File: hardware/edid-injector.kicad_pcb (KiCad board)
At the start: 2 copper layers, 42 parts, among them SW1 SW_PUSH, U1 C8051F381/3/5/7/C-GQ

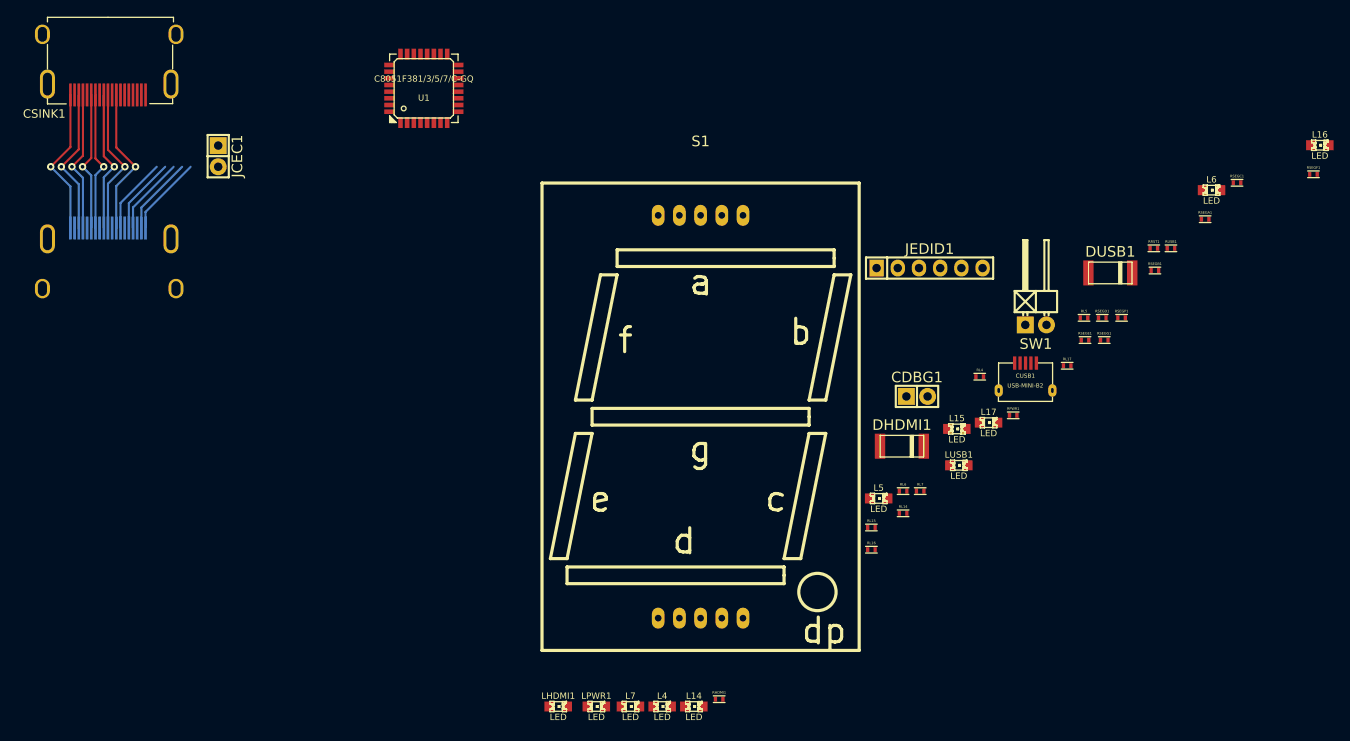
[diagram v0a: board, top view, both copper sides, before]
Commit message: Begin PCB layout - cleaning up rats nest
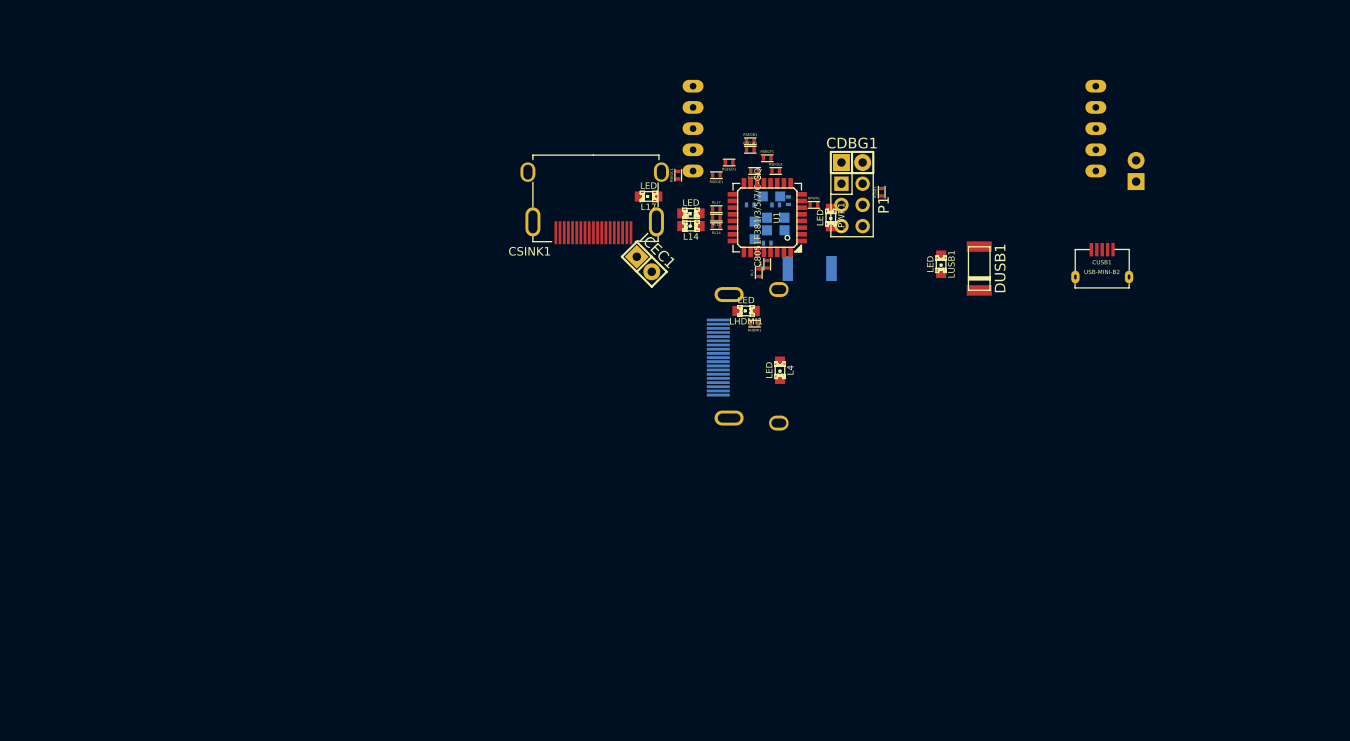
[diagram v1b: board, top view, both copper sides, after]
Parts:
- removed JEDID1: CONN_01X06, Pin_Headers:Pin_Header_Straight_1x06
- added P1: CONN_02X03, Pin_Headers:Pin_Header_Straight_2x03, F.Cu at (141.7, 67.8)
- DHDMI1, L16, L5, L6, L7, RL16, RL5, RL6, RRST1, S1, SW1: moved to B.Cu
- moved CSRC1 75.8 mm to (127.0, 86.1), turned to 270 degrees
- moved RSEGC1 67.0 mm to (120.9, 64.3), turned to 90 degrees
- moved L16 65.8 mm to (132.6, 69.3), turned to 180 degrees
- moved RSEGF1 65.5 mm to (131.6, 62.2)
- moved LPWR1 65.0 mm to (139.2, 69.3), turned to 270 degrees
- moved CSINK1 60.5 mm to (110.7, 69.8)
- moved L7 59.0 mm to (130.0, 70.9), turned to 90 degrees
- moved L14 57.6 mm to (122.4, 70.4), turned to 180 degrees
- moved RSEGA1 55.1 mm to (129.5, 61.2)
- moved JCEC1 52.7 mm to (116.8, 74.9), turned to 315 degrees
- moved LHDMI1 52.5 mm to (129.0, 80.5), turned to 180 degrees
- moved L6 52.4 mm to (132.6, 70.9)
- moved RSEGB1 50.9 mm to (129.5, 60.2)
- moved L17 48.9 mm to (117.3, 66.8), turned to 180 degrees
- moved RSEGD1 48.4 mm to (127.0, 62.7), turned to 180 degrees
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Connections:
- CSINK1 pad 14: Net-(CSINK1-Pad14) -> (no net)
- CSRC1 pad 14: Net-(CSRC1-Pad14) -> (no net)
- CUSB1 pad 4: Net-(CUSB1-Pad4) -> (no net)
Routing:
- net /D2+: track 17.9 -> 0.00 mm, vias 1 -> 0
- net /CLK-: track 17.8 -> 0.00 mm, vias 1 -> 0
- net /D2-: track 17.7 -> 0.00 mm, vias 1 -> 0
- net /CLK+: track 17.6 -> 0.00 mm, vias 1 -> 0
- net /D1+: track 17.0 -> 0.00 mm, vias 1 -> 0
- net /D0-: track 17.0 -> 0.00 mm, vias 1 -> 0
- net /D1-: track 16.8 -> 0.00 mm, vias 1 -> 0
- net /D0+: track 16.8 -> 0.00 mm, vias 1 -> 0
- net /SRC_HPD: track 9.58 -> 0.00 mm
- net /VHDMI: track 9.36 -> 0.00 mm
- net /SRC_SDA: track 9.35 -> 0.00 mm
- net /SRC_SCL: track 9.14 -> 0.00 mm
- net /SRC_CEC: track 9.13 -> 0.00 mm

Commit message: Converging on sane placement for parts
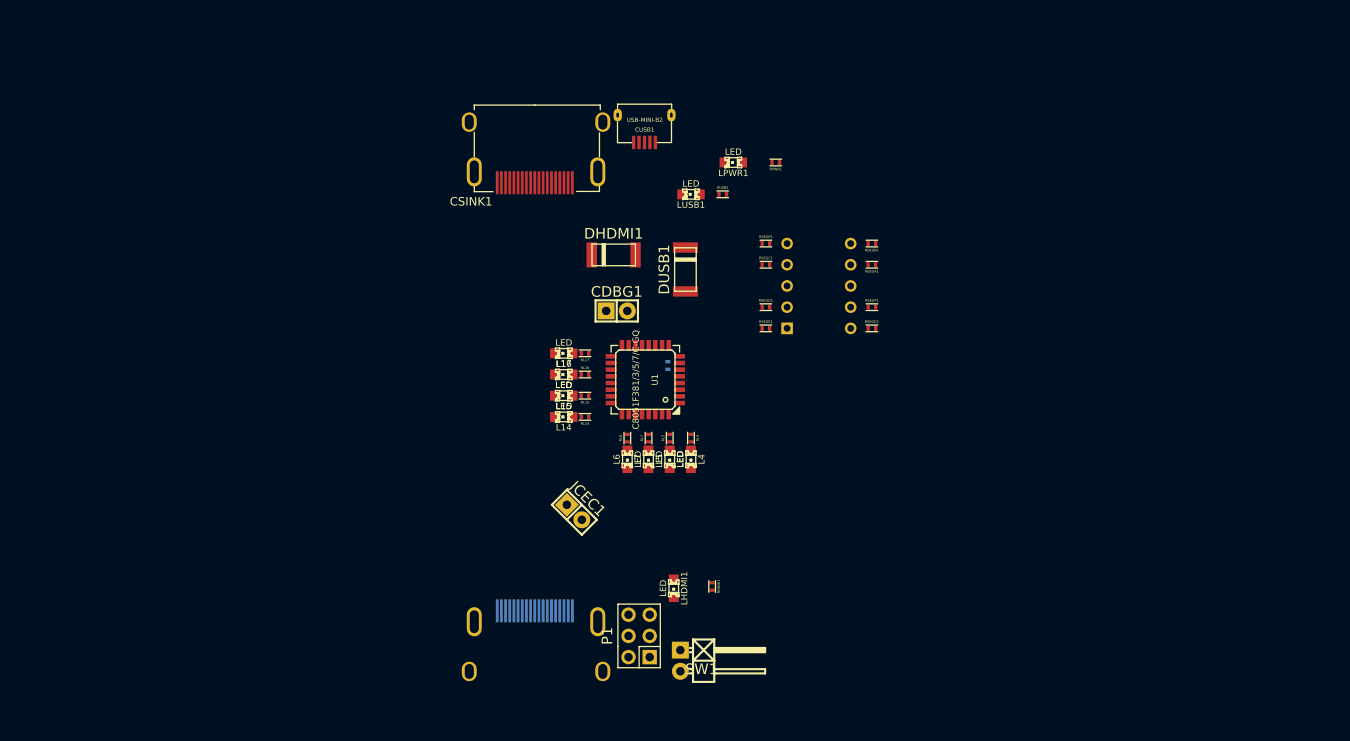
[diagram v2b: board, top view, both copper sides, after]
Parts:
- DHDMI1, L16, L5, L6, L7, RL16, RL5, RL6, SW1: moved to F.Cu
- S1: footprint Displays_7-Segment:7SegmentLED_SBC18-11EGWA -> Sockets_DIP:DIP-10__300
- moved SW1 80.2 mm to (121.2, 122.4), turned to 270 degrees
- moved CUSB1 58.2 mm to (116.9, 57.1), turned to 180 degrees
- moved P1 57.6 mm to (116.2, 119.5), turned to 90 degrees
- moved CSRC1 39.3 mm to (103.7, 117.8), turned to 180 degrees
- moved DUSB1 35.2 mm to (121.8, 75.6), turned to 90 degrees
- moved LHDMI1 34.4 mm to (120.4, 113.8), turned to 270 degrees
- moved L5 33.8 mm to (119.9, 98.3), turned to 270 degrees
- moved CDBG1 33.3 mm to (113.5, 80.5)
- moved L6 32.7 mm to (114.8, 98.3), turned to 270 degrees
- moved RHDMI1 31.9 mm to (125.0, 113.5), turned to 270 degrees
- moved L16 31.6 mm to (107.2, 88.1)
- moved LUSB1 31.1 mm to (122.4, 66.5), turned to 180 degrees
- moved JCEC1 30.9 mm to (108.5, 104.6)
- moved RL5 30.7 mm to (119.9, 95.8), turned to 270 degrees
- moved L7 30.2 mm to (117.3, 98.3), turned to 270 degrees
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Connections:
- CSINK1 pad 14: (no net) -> Net-(CSINK1-Pad14)
- CSRC1 pad 14: (no net) -> Net-(CSRC1-Pad14)
- CUSB1 pad 4: (no net) -> Net-(CUSB1-Pad4)
- P1 pad 1: (no net) -> Net-(P1-Pad1)
- P1 pad 2: (no net) -> Net-(P1-Pad2)
- P1 pad 3: (no net) -> Net-(P1-Pad3)
- P1 pad 4: (no net) -> Net-(P1-Pad4)
- P1 pad 6: (no net) -> Net-(P1-Pad6)

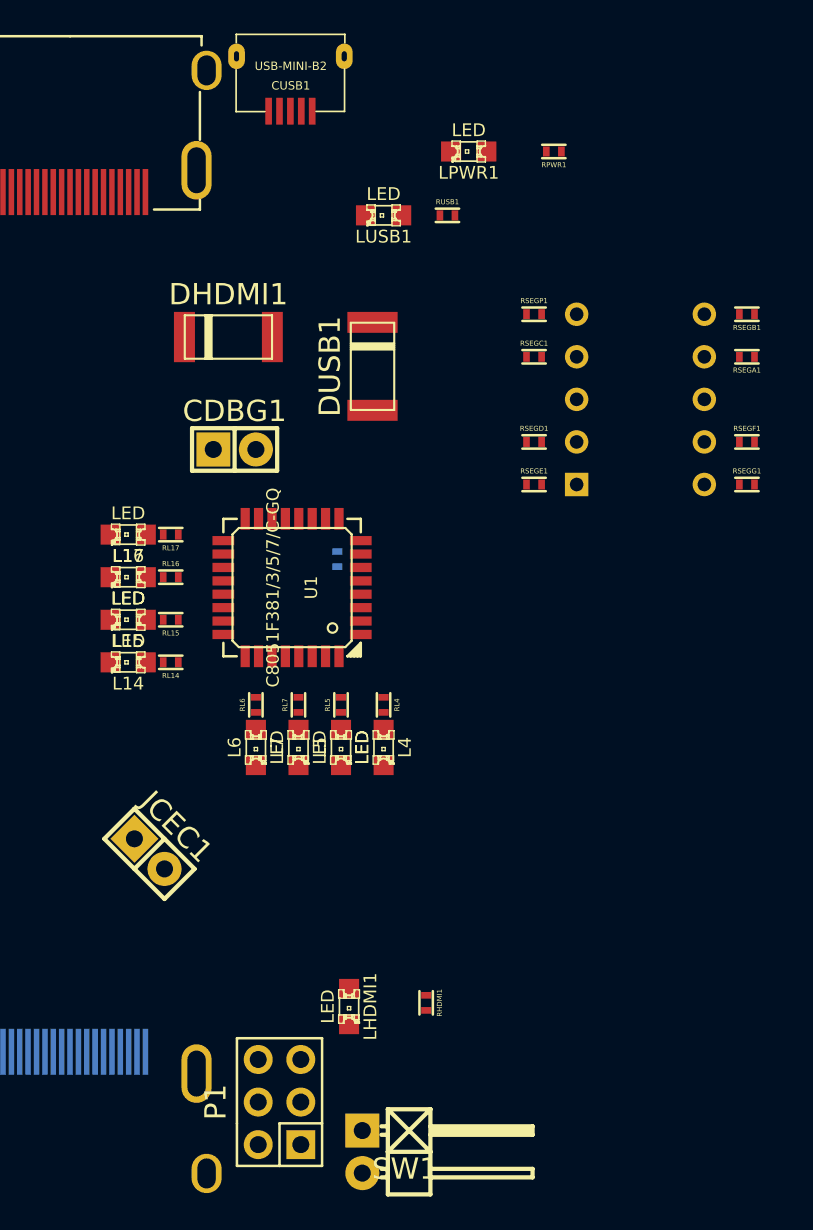
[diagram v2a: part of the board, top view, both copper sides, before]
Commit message: Closer to an autorouter-friendly layout.
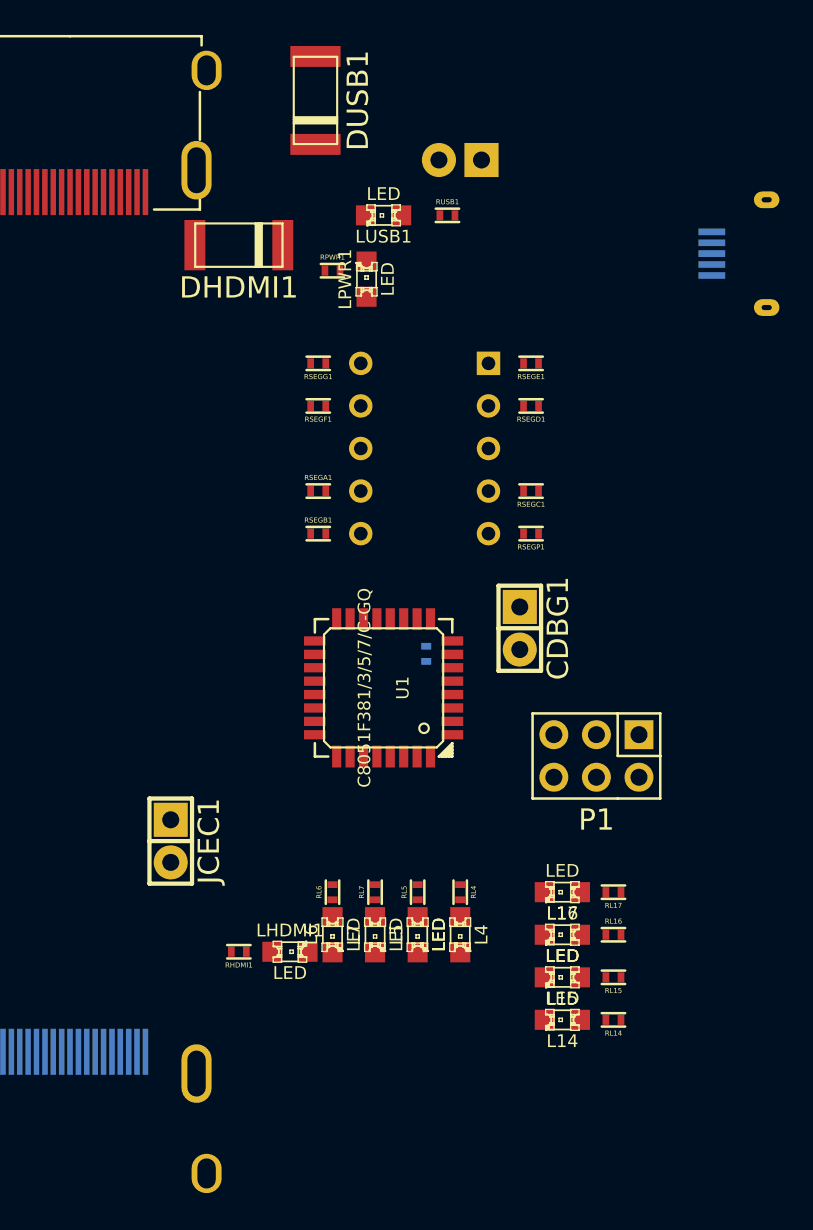
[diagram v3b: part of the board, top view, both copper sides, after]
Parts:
- CUSB1, SW1: moved to B.Cu
- moved SW1 59.5 mm to (127.0, 63.2), turned to 180 degrees
- moved RL14 34.0 mm to (136.1, 114.6)
- moved RL15 34.0 mm to (136.1, 112.0)
- moved RL16 34.0 mm to (136.1, 109.5)
- moved RL17 34.0 mm to (136.1, 106.9)
- moved L14 33.6 mm to (133.1, 114.6)
- moved L15 33.6 mm to (133.1, 112.0)
- moved L16 33.6 mm to (133.1, 109.5)
- moved L17 33.6 mm to (133.1, 106.9)
- moved CUSB1 30.8 mm to (145.3, 68.8), turned to 270 degrees
- moved RSEGB1 28.7 mm to (118.5, 85.5), turned to 0 degrees
- moved P1 28.0 mm to (135.1, 98.8), turned to 180 degrees
- moved RSEGA1 26.8 mm to (118.5, 83.0), turned to 0 degrees
- moved RSEGG1 26.6 mm to (118.5, 75.4), turned to 180 degrees
- moved RSEGF1 25.7 mm to (118.5, 77.9), turned to 180 degrees
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
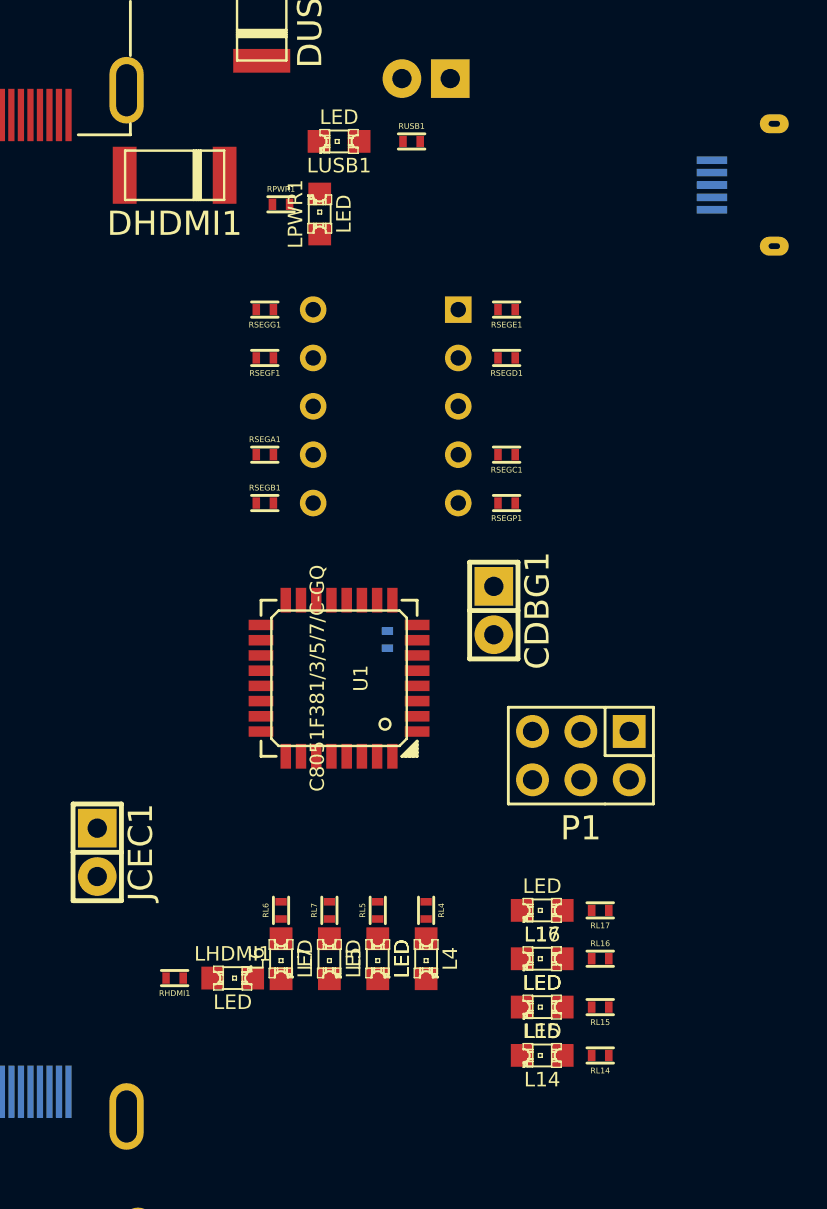
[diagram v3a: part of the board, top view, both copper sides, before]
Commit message: Better layout for PCB - autorouter is at -7 traces
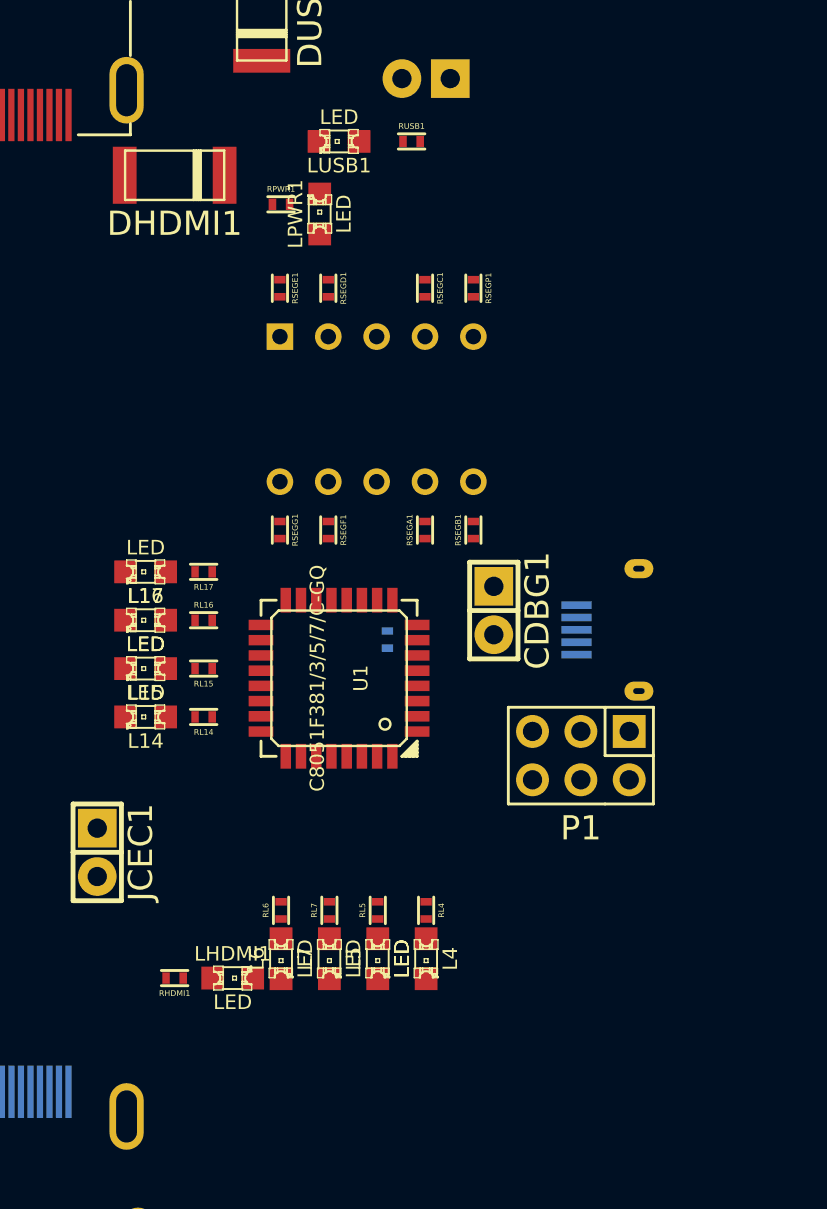
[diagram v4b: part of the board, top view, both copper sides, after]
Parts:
- moved L14 27.4 mm to (112.3, 96.8)
- moved L15 27.4 mm to (112.3, 94.2)
- moved L16 27.4 mm to (112.3, 91.7)
- moved L17 27.4 mm to (112.3, 89.2)
- moved RL14 27.4 mm to (115.3, 96.8)
- moved RL15 27.4 mm to (115.3, 94.2)
- moved RL16 27.4 mm to (115.3, 91.7)
- moved RL17 27.4 mm to (115.3, 89.2)
- moved CUSB1 24.4 mm to (138.2, 92.2)
- moved RSEGE1 12.0 mm to (119.3, 74.3), turned to 270 degrees
- moved RSEGG1 11.6 mm to (119.3, 87.0), turned to 270 degrees
- moved RSEGP1 11.4 mm to (129.5, 74.3), turned to 270 degrees
- moved RSEGB1 11.0 mm to (129.5, 87.0), turned to 90 degrees
- moved RSEGD1 10.1 mm to (121.9, 74.3), turned to 270 degrees
- moved RSEGC1 9.74 mm to (126.9, 74.3), turned to 270 degrees
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
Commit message: Preliminary route.
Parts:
- moved JCEC1 3.05 mm to (106.7, 103.9)
- moved L15 0.51 mm to (112.3, 94.7)
- moved L17 0.51 mm to (112.3, 89.7)
- moved LHDMI1 0.51 mm to (116.8, 111.0)
- moved RHDMI1 0.51 mm to (113.8, 111.0)
- moved RL15 0.51 mm to (115.3, 94.7)
- moved RL17 0.51 mm to (115.3, 89.7)
- moved RRST1 0.51 mm to (125.0, 93.2)
- moved RSEGC1 0.51 mm to (126.9, 74.8)
- moved RSEGD1 0.51 mm to (121.9, 74.8)
- moved RSEGE1 0.51 mm to (119.3, 74.8)
- moved RSEGP1 0.51 mm to (129.5, 74.8)
- moved CDBG1 0.51 mm to (130.6, 91.7)
- moved CUSB1 0.51 mm to (138.2, 92.7)
- moved L14 0.51 mm to (112.3, 97.3)
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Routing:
- net GND: track 0.00 -> 239.2 mm, vias 0 -> 6
- net /SINK_SCL: track 0.00 -> 83.0 mm, vias 0 -> 2
- net /CLK-: track 0.00 -> 71.5 mm, vias 0 -> 3
- net /D0+: track 0.00 -> 67.4 mm, vias 0 -> 3
- net /D1-: track 0.00 -> 64.1 mm, vias 0 -> 1
- net Net-(CDBG1-Pad2): track 0.00 -> 61.6 mm, vias 0 -> 4
- net /VHDMI: track 0.00 -> 59.6 mm, vias 0 -> 1
- net /D1+: track 0.00 -> 59.5 mm, vias 0 -> 1
- net /SINK_CEC: track 0.00 -> 57.7 mm, vias 0 -> 3
- net /VUSB: track 0.00 -> 54.5 mm, vias 0 -> 1
- net /VCC5V0: track 0.00 -> 53.2 mm, vias 0 -> 2
- net /D2-: track 0.00 -> 53.1 mm, vias 0 -> 1
- net /D2+: track 0.00 -> 52.6 mm, vias 0 -> 1
- net /D0-: track 0.00 -> 52.5 mm, vias 0 -> 1
- net /CLK+: track 0.00 -> 51.6 mm, vias 0 -> 1
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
